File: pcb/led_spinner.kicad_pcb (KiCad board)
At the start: 2 copper layers, 48.3 x 48.3 mm, 43 parts, among them CON1 AVR-ISP-6, J1 SERIAL, J2 SPARE, J3 TILT, SW1 SW_PUSH_ALT, U1 ATMEGA48_88_168_328P-32SMD

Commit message: Fix LED/resistor pairs that didn't have the correct ends together.
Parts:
- turned R13 to 225 degrees
- turned R2 to 90 degrees
- turned R5 to 135 degrees
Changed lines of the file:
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@@
   )
   (module w_smd_resistors:r_0805 (layer F.Cu)
-    (at 173.99 106.68 270)
-    (descr "SMT resistor, 0805")
-    (fp_text reference R2 (at 0 -0.9906 270) (layer F.SilkS)
-      (effects (font (size 0.29972 0.29972) (thickness 0.06096)))
-    )
-    (fp_text value R (at 0 0.9906 270) (layer F.SilkS) hide
-      (effects (font (size 0.29972 0.29972) (thickness 0.06096)))
-    )
-    (fp_line (start 0.635 -0.635) (end 0.635 0.635) (layer F.SilkS) (width 0.127))
-    (fp_line (start -0.635 -0.635) (end -0.635 0.6096) (layer F.SilkS) (width 0.127))
-    (fp_line (start -1.016 -0.635) (end 1.016 -0.635) (layer F.SilkS) (width 0.127))
-    (fp_line (start 1.016 -0.635) (end 1.016 0.635) (layer F.SilkS) (width 0.127))
-    (fp_line (start 1.016 0.635) (end -1.016 0.635) (layer F.SilkS) (width 0.127))
-    (fp_line (start -1.016 0.635) (end -1.016 -0.635) (layer F.SilkS) (width 0.127))
-    (pad 1 smd rect (at 0.9525 0 270) (size 1.30048 1.4986) (layers F.Cu F.Paste F.Mask)
+    (at 173.99 106.68 90)
+    (descr "SMT resistor, 0805")
+    (fp_text reference R2 (at 0 -0.9906 90) (layer F.SilkS)
+      (effects (font (size 0.29972 0.29972) (thickness 0.06096)))
+    )
+    (fp_text value R (at 0 0.9906 90) (layer F.SilkS) hide
+      (effects (font (size 0.29972 0.29972) (thickness 0.06096)))
+    )
+    (fp_line (start 0.635 -0.635) (end 0.635 0.635) (layer F.SilkS) (width 0.127))
+    (fp_line (start -0.635 -0.635) (end -0.635 0.6096) (layer F.SilkS) (width 0.127))
+    (fp_line (start -1.016 -0.635) (end 1.016 -0.635) (layer F.SilkS) (width 0.127))
+    (fp_line (start 1.016 -0.635) (end 1.016 0.635) (layer F.SilkS) (width 0.127))
+    (fp_line (start 1.016 0.635) (end -1.016 0.635) (layer F.SilkS) (width 0.127))
+    (fp_line (start -1.016 0.635) (end -1.016 -0.635) (layer F.SilkS) (width 0.127))
+    (pad 1 smd rect (at 0.9525 0 90) (size 1.30048 1.4986) (layers F.Cu F.Paste F.Mask)
       (net 29 "Net-(LD1-Pad1)"))
-    (pad 2 smd rect (at -0.9525 0 270) (size 1.30048 1.4986) (layers F.Cu F.Paste F.Mask)
+    (pad 2 smd rect (at -0.9525 0 90) (size 1.30048 1.4986) (layers F.Cu F.Paste F.Mask)
       (net 18 /FW))
     (model walter/smd_resistors/r_0805.wrl
@@
   )
   (module w_smd_resistors:r_0805 (layer F.Cu)
-    (at 180.34 120.65 315)
-    (descr "SMT resistor, 0805")
-    (fp_text reference R5 (at 0 -0.9906 315) (layer F.SilkS)
-      (effects (font (size 0.29972 0.29972) (thickness 0.06096)))
-    )
-    (fp_text value R (at 0 0.9906 315) (layer F.SilkS) hide
-      (effects (font (size 0.29972 0.29972) (thickness 0.06096)))
-    )
-    (fp_line (start 0.635 -0.635) (end 0.635 0.635) (layer F.SilkS) (width 0.127))
-    (fp_line (start -0.635 -0.635) (end -0.635 0.6096) (layer F.SilkS) (width 0.127))
-    (fp_line (start -1.016 -0.635) (end 1.016 -0.635) (layer F.SilkS) (width 0.127))
-    (fp_line (start 1.016 -0.635) (end 1.016 0.635) (layer F.SilkS) (width 0.127))
-    (fp_line (start 1.016 0.635) (end -1.016 0.635) (layer F.SilkS) (width 0.127))
-    (fp_line (start -1.016 0.635) (end -1.016 -0.635) (layer F.SilkS) (width 0.127))
-    (pad 1 smd rect (at 0.9525 0 315) (size 1.30048 1.4986) (layers F.Cu F.Paste F.Mask)
+    (at 180.34 120.65 135)
+    (descr "SMT resistor, 0805")
+    (fp_text reference R5 (at 0 -0.9906 135) (layer F.SilkS)
+      (effects (font (size 0.29972 0.29972) (thickness 0.06096)))
+    )
+    (fp_text value R (at 0 0.9906 135) (layer F.SilkS) hide
+      (effects (font (size 0.29972 0.29972) (thickness 0.06096)))
+    )
+    (fp_line (start 0.635 -0.635) (end 0.635 0.635) (layer F.SilkS) (width 0.127))
+    (fp_line (start -0.635 -0.635) (end -0.635 0.6096) (layer F.SilkS) (width 0.127))
+    (fp_line (start -1.016 -0.635) (end 1.016 -0.635) (layer F.SilkS) (width 0.127))
+    (fp_line (start 1.016 -0.635) (end 1.016 0.635) (layer F.SilkS) (width 0.127))
+    (fp_line (start 1.016 0.635) (end -1.016 0.635) (layer F.SilkS) (width 0.127))
+    (fp_line (start -1.016 0.635) (end -1.016 -0.635) (layer F.SilkS) (width 0.127))
+    (pad 1 smd rect (at 0.9525 0 135) (size 1.30048 1.4986) (layers F.Cu F.Paste F.Mask)
       (net 39 "Net-(LD4-Pad1)"))
-    (pad 2 smd rect (at -0.9525 0 315) (size 1.30048 1.4986) (layers F.Cu F.Paste F.Mask)
+    (pad 2 smd rect (at -0.9525 0 135) (size 1.30048 1.4986) (layers F.Cu F.Paste F.Mask)
       (net 17 /FSW))
     (model walter/smd_resistors/r_0805.wrl
@@
   )
   (module w_smd_resistors:r_0805 (layer F.Cu)
-    (at 208.28 120.65 45)
-    (descr "SMT resistor, 0805")
-    (fp_text reference R13 (at 0 -0.9906 45) (layer F.SilkS)
-      (effects (font (size 0.29972 0.29972) (thickness 0.06096)))
-    )
-    (fp_text value R (at 0 0.9906 45) (layer F.SilkS) hide
-      (effects (font (size 0.29972 0.29972) (thickness 0.06096)))
-    )
-    (fp_line (start 0.635 -0.635) (end 0.635 0.635) (layer F.SilkS) (width 0.127))
-    (fp_line (start -0.635 -0.635) (end -0.635 0.6096) (layer F.SilkS) (width 0.127))
-    (fp_line (start -1.016 -0.635) (end 1.016 -0.635) (layer F.SilkS) (width 0.127))
-    (fp_line (start 1.016 -0.635) (end 1.016 0.635) (layer F.SilkS) (width 0.127))
-    (fp_line (start 1.016 0.635) (end -1.016 0.635) (layer F.SilkS) (width 0.127))
-    (fp_line (start -1.016 0.635) (end -1.016 -0.635) (layer F.SilkS) (width 0.127))
-    (pad 1 smd rect (at 0.9525 0 45) (size 1.30048 1.4986) (layers F.Cu F.Paste F.Mask)
+    (at 208.28 120.65 225)
+    (descr "SMT resistor, 0805")
+    (fp_text reference R13 (at 0 -0.9906 225) (layer F.SilkS)
+      (effects (font (size 0.29972 0.29972) (thickness 0.06096)))
+    )
+    (fp_text value R (at 0 0.9906 225) (layer F.SilkS) hide
+      (effects (font (size 0.29972 0.29972) (thickness 0.06096)))
+    )
+    (fp_line (start 0.635 -0.635) (end 0.635 0.635) (layer F.SilkS) (width 0.127))
+    (fp_line (start -0.635 -0.635) (end -0.635 0.6096) (layer F.SilkS) (width 0.127))
+    (fp_line (start -1.016 -0.635) (end 1.016 -0.635) (layer F.SilkS) (width 0.127))
+    (fp_line (start 1.016 -0.635) (end 1.016 0.635) (layer F.SilkS) (width 0.127))
+    (fp_line (start 1.016 0.635) (end -1.016 0.635) (layer F.SilkS) (width 0.127))
+    (fp_line (start -1.016 0.635) (end -1.016 -0.635) (layer F.SilkS) (width 0.127))
+    (pad 1 smd rect (at 0.9525 0 225) (size 1.30048 1.4986) (layers F.Cu F.Paste F.Mask)
       (net 32 "Net-(LD12-Pad1)"))
-    (pad 2 smd rect (at -0.9525 0 45) (size 1.30048 1.4986) (layers F.Cu F.Paste F.Mask)
+    (pad 2 smd rect (at -0.9525 0 225) (size 1.30048 1.4986) (layers F.Cu F.Paste F.Mask)
       (net 16 /FSE))
     (model walter/smd_resistors/r_0805.wrl

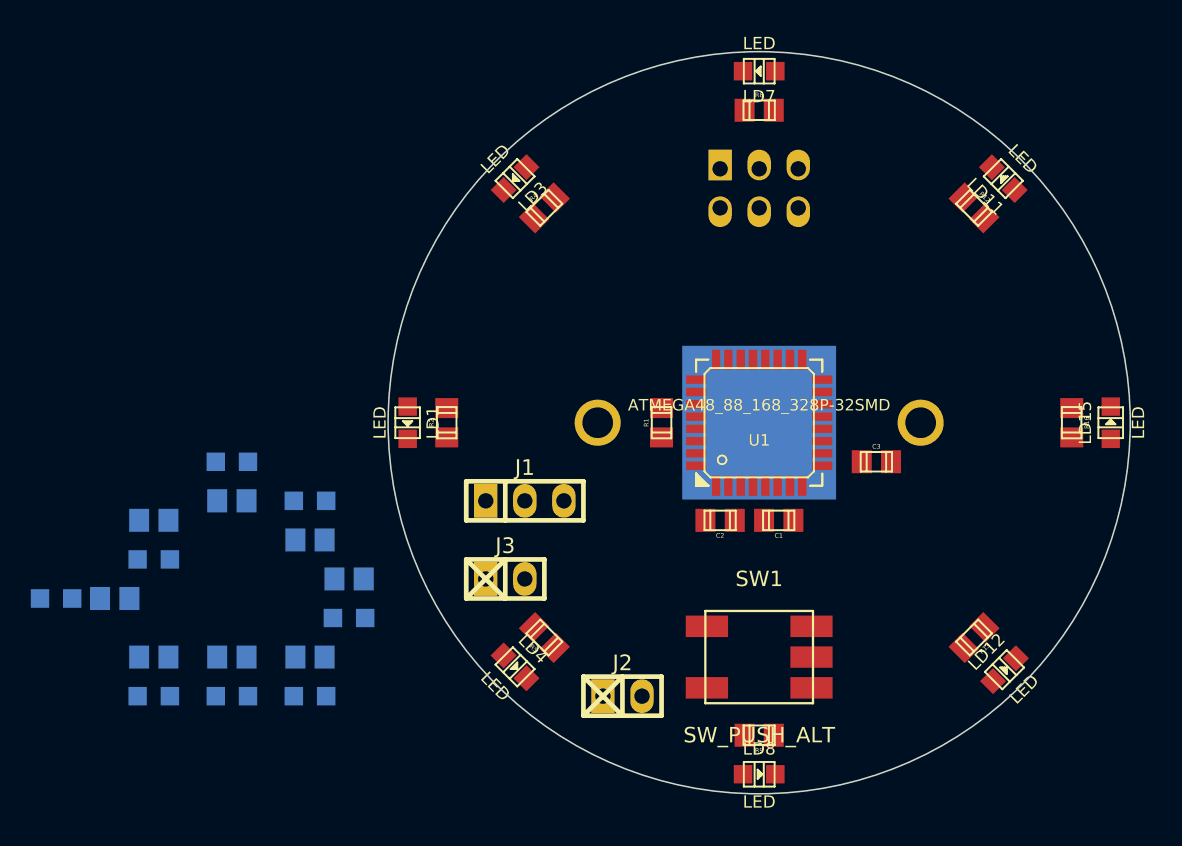
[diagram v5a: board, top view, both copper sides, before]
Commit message: Add tracks between LED and resistors.
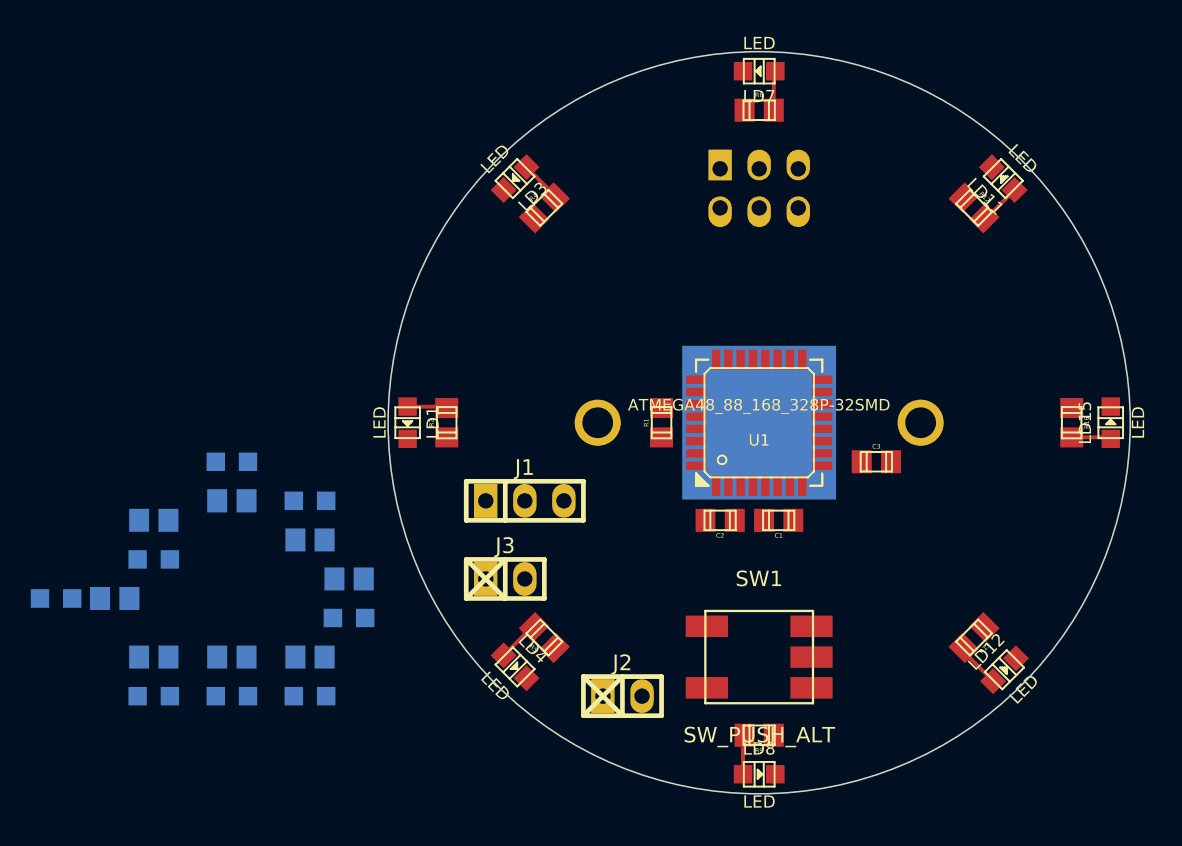
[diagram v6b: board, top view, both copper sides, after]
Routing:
- net Net-(LD12-Pad1): track 0.00 -> 2.95 mm
- net Net-(LD11-Pad1): track 0.00 -> 2.73 mm
- net Net-(LD4-Pad1): track 0.00 -> 2.73 mm
- net Net-(LD3-Pad1): track 0.00 -> 2.73 mm
- net Net-(LD1-Pad1): track 0.00 -> 2.58 mm
- net Net-(LD7-Pad1): track 0.00 -> 2.58 mm
- net Net-(LD15-Pad1): track 0.00 -> 2.58 mm
- net Net-(LD8-Pad1): track 0.00 -> 2.58 mm
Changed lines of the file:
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@@
   (general
     (links 77)
-    (no_connects 77)
-    (area 0 0 0 0)
+    (no_connects 69)
+    (area 146.68754 80.98028 223.620001 135.990001)
     (thickness 1.6)
     (drawings 7)
-    (tracks 0)
+    (tracks 16)
     (zones 0)
     (modules 43)
@@
   (gr_line (start 194.31 132.08) (end 194.31 135.89) (angle 90) (layer Dwgs.User) (width 0.2))
   (gr_circle (center 194.31 106.68) (end 218.44 106.68) (layer Edge.Cuts) (width 0.1))
+  (segment (start 171.45 105.63098) (end 173.89348 105.63098) (width 0.254) (layer F.Cu) (net 29) (status C00000))
+  (segment (start 173.89348 105.63098) (end 173.99 105.7275) (width 0.254) (layer F.Cu) (net 29) (status C00000))
+  (segment (start 208.953519 93.383519) (end 209.090019 93.383519) (width 0.254) (layer F.Cu) (net 31))
+  (segment (start 209.090019 93.383519) (end 210.926769 91.546769) (width 0.254) (layer F.Cu) (net 31))
+  (segment (start 207.606481 121.323519) (end 207.606481 121.568968) (width 0.254) (layer F.Cu) (net 32) (status C00000))
+  (segment (start 207.606481 121.568968) (end 209.520269 123.482756) (width 0.254) (layer F.Cu) (net 32) (status C00000))
+  (segment (start 214.63 107.6325) (end 217.07348 107.6325) (width 0.254) (layer F.Cu) (net 35) (status C00000))
+  (segment (start 217.07348 107.6325) (end 217.17 107.72902) (width 0.254) (layer F.Cu) (net 35) (status C00000))
+  (segment (start 181.013519 92.036481) (end 181.013519 91.899981) (width 0.254) (layer F.Cu) (net 38) (status C00000))
+  (segment (start 181.013519 91.899981) (end 179.176769 90.063231) (width 0.254) (layer F.Cu) (net 38) (status C00000))
+  (segment (start 179.666481 119.976481) (end 179.529981 119.976481) (width 0.254) (layer F.Cu) (net 39) (status C00000))
+  (segment (start 179.529981 119.976481) (end 177.693231 121.813231) (width 0.254) (layer F.Cu) (net 39) (status C00000))
+  (segment (start 195.2625 86.36) (end 195.2625 83.91652) (width 0.254) (layer F.Cu) (net 42) (status C00000))
+  (segment (start 195.2625 83.91652) (end 195.35902 83.82) (width 0.254) (layer F.Cu) (net 42) (status C00000))
+  (segment (start 193.26098 129.54) (end 193.26098 127.09652) (width 0.254) (layer F.Cu) (net 43) (status C00000))
+  (segment (start 193.26098 127.09652) (end 193.3575 127) (width 0.254) (layer F.Cu) (net 43) (status C00000))
 )

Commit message: Lay tracks to decoupling caps, reset pull up resistor and signal connections to all front LEDs.
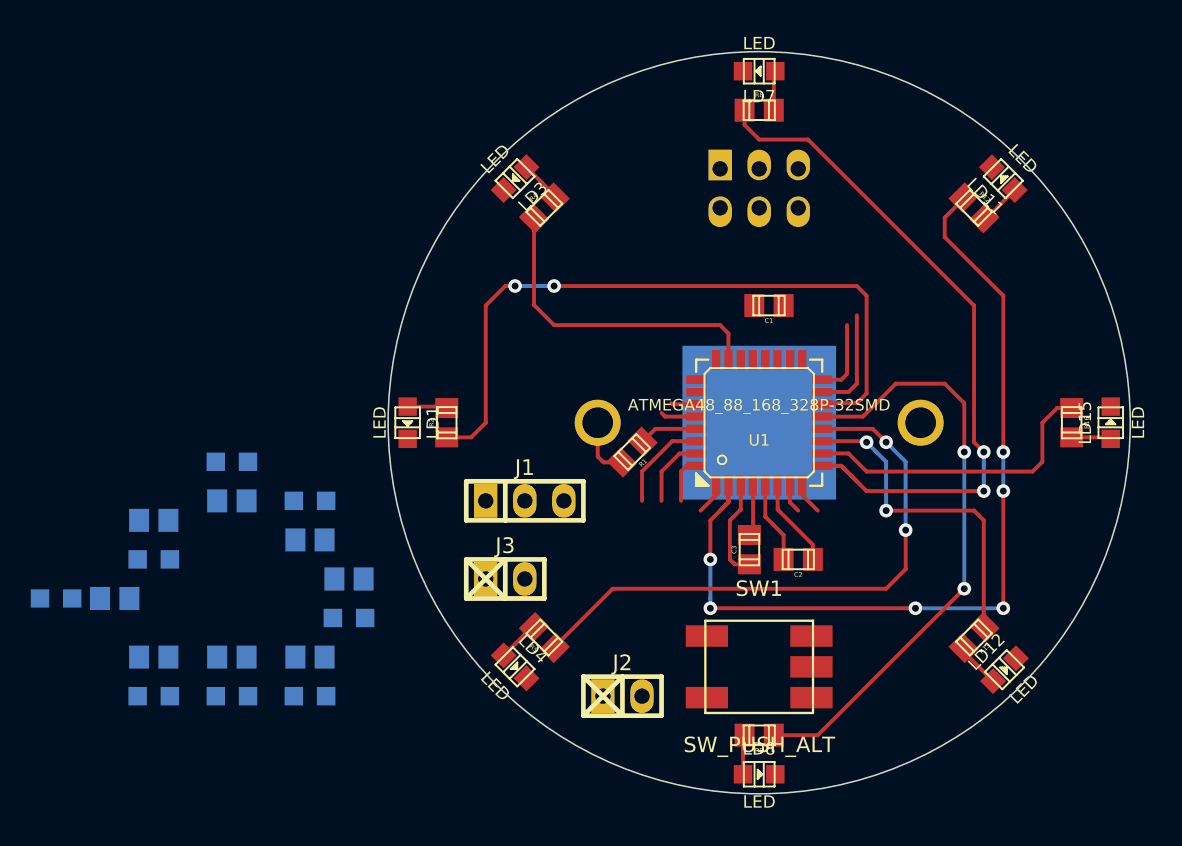
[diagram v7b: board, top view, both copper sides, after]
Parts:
- moved C1 14.0 mm to (194.9, 99.1)
- moved C3 10.0 mm to (193.7, 114.9), turned to 90 degrees
- moved C2 5.68 mm to (196.8, 115.6)
- moved R1 2.69 mm to (186.1, 108.6), turned to 225 degrees
- moved SW1 0.64 mm to (194.3, 122.6)
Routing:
- net /FNE: track 0.00 -> 58.1 mm, vias 0 -> 6
- net /FN: track 0.00 -> 45.7 mm, vias 0 -> 2
- net /FW: track 0.00 -> 45.6 mm, vias 0 -> 2
- net /FS: track 0.00 -> 39.0 mm, vias 0 -> 2
- net /FSW: track 0.00 -> 38.3 mm, vias 0 -> 2
- net /FE: track 0.00 -> 21.8 mm
- net /FSE: track 0.00 -> 21.5 mm, vias 0 -> 2
- net /FNW: track 0.00 -> 20.8 mm
- net +BATT: track 0.00 -> 13.0 mm
- net GND: track 0.00 -> 11.8 mm
- net /MOSI: track 0.00 -> 6.92 mm
- net /RXD: track 0.00 -> 6.24 mm
- net /MISO: track 0.00 -> 4.95 mm
- net /TXD: track 0.00 -> 4.64 mm
- net /~RESET: track 0.00 -> 3.83 mm
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
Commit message: Route signals to back-side LEDs. Route signals to connectors except for ICSP. Route button.
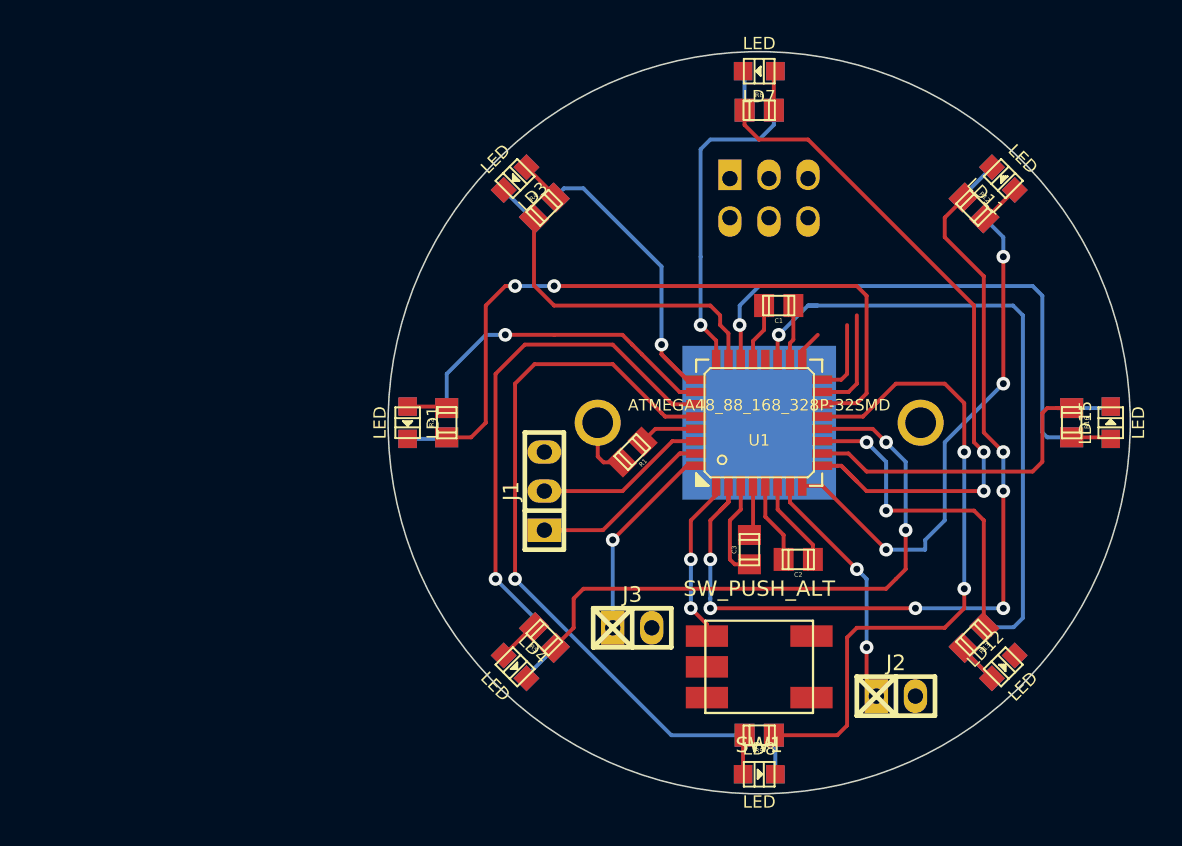
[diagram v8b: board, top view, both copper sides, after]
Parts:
- moved LD2 69.5 mm to (217.2, 106.7), turned to 270 degrees
- moved LD5 64.7 mm to (210.2, 90.8), turned to 315 degrees
- moved R3 63.3 mm to (214.6, 106.7), turned to 90 degrees
- moved R6 60.8 mm to (208.3, 92.7), turned to 135 degrees
- moved LD6 55.7 mm to (210.2, 122.6), turned to 45 degrees
- moved R7 53.9 mm to (208.3, 120.7), turned to 225 degrees
- moved LD9 53.2 mm to (194.3, 83.8), turned to 0 degrees
- moved R10 49.4 mm to (194.3, 86.4), turned to 180 degrees
- moved LD10 39.9 mm to (194.3, 129.5)
- moved R11 37.5 mm to (194.3, 127.0)
- moved LD13 36.2 mm to (178.4, 90.8), turned to 45 degrees
- moved R14 32.9 mm to (180.3, 92.7), turned to 225 degrees
- moved J2 17.8 mm to (203.2, 124.5)
- moved LD14 17.2 mm to (178.4, 122.6), turned to 135 degrees
- moved R15 16.5 mm to (180.3, 120.7), turned to 315 degrees
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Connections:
- SW1 pad 1: GND -> /BUTTON
- SW1 pad 3: /BUTTON -> GND
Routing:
- net /BS: track 2.35 -> 45.5 mm, vias 0 -> 1
- net /BSW: track 0.00 -> 41.6 mm, vias 0 -> 1
- net /BW: track 0.00 -> 35.0 mm, vias 0 -> 1
- net /BNW: track 2.03 -> 33.9 mm, vias 0 -> 3
- net /BSE: track 1.64 -> 33.1 mm, vias 0 -> 1
- net /BE: track 0.00 -> 21.0 mm, vias 0 -> 1
- net /BN: track 0.00 -> 20.5 mm, vias 0 -> 1
- net /BNE: track 0.00 -> 20.3 mm, vias 0 -> 1
- net Net-(J2-Pad1): track 1.84 -> 16.0 mm, vias 0 -> 2
- net Net-(J3-Pad1): track 3.04 -> 13.1 mm, vias 0 -> 1
- net /BUTTON: track 2.03 -> 10.9 mm, vias 0 -> 2
- net /TXD: track 4.64 -> 11.9 mm
- net /RXD: track 6.24 -> 11.2 mm
- net /FS: track 39.0 -> 43.1 mm
- net GND: track 11.8 -> 15.6 mm
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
